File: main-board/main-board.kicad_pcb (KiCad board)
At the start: 2 copper layers, 81.6 x 87.9 mm, 67 parts, among them J1 MOTOR0, J10 PROGRAMMER, J11 CAM0, J12 CAM1, J13 CAM2, J14 CAM3, J15 CAM4, J16 CAM5, J17 CAM6, J18 CAM7, J19 PowerBoard Interface, J2 MOTOR1, J20 IMU Breakout, J21 ICSP (DO NOT POPULATE), J22 PLAN (US)B PINS, J3 MOTOR2, J4 MOTOR3, J5 TETHER INTERFACE, J6 MOTOR4, J7 MOTOR5, J8 MOTOR6, J9 MOTOR7, SW1 SW_SPST, U1 MCP2515-EST, U10 MAX4449ESE+, U2 ATA6560, U3 ATmega2560-16AU | Main Proc, U4 MC14051B, U5 MC14051B, U6 MAX490E, U7 LTC1983ES6-5-TRPBF, U8 MAX4449ESE+, Y1 20MHz, Y2 20MHz

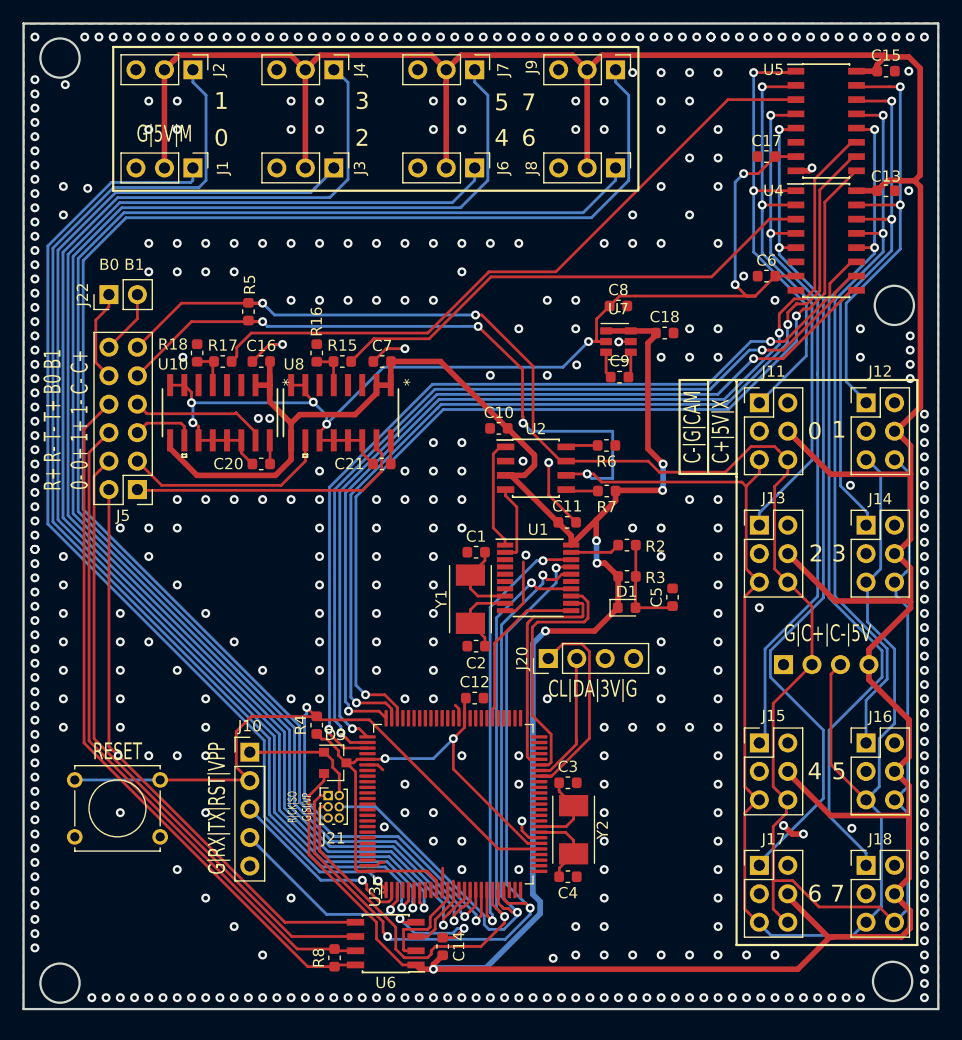
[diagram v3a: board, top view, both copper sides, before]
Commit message: Replaced moutning holes drawn in edge cuts with real holes and regenerated all gerbers
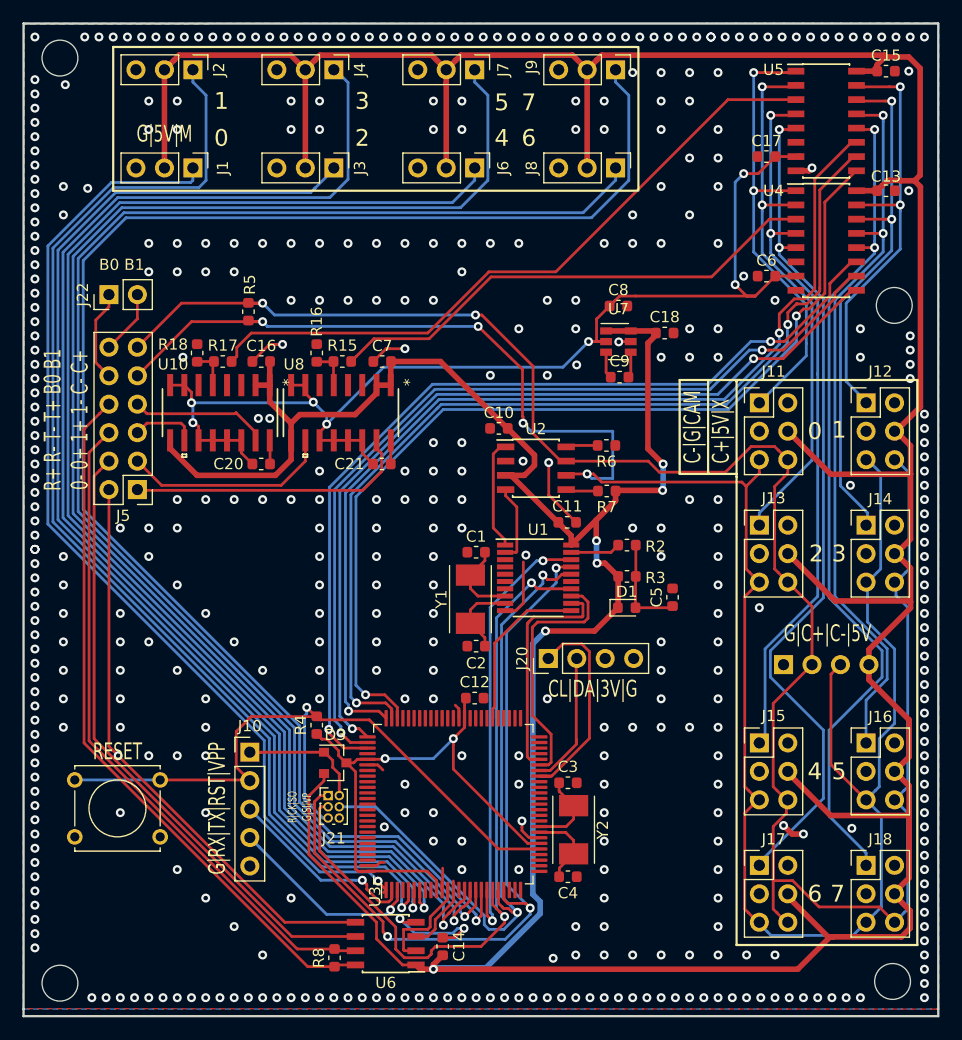
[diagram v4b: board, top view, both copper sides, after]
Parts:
- added REF**: MountingHole_3.2mm_M3, MountingHole:MountingHole_3.2mm_M3, F.Cu at (68.3, 127.0)
- added REF**: MountingHole_3.2mm_M3, MountingHole:MountingHole_3.2mm_M3, F.Cu at (142.6, 126.8)
- added REF**: MountingHole_3.2mm_M3, MountingHole:MountingHole_3.2mm_M3, F.Cu at (142.7, 66.5)
- added REF**: MountingHole_3.2mm_M3, MountingHole:MountingHole_3.2mm_M3, F.Cu at (68.3, 44.4)
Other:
- board size 81.6 x 87.9 mm -> 81.6 x 88.6 mm
